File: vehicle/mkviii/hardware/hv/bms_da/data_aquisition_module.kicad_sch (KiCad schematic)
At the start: 70 parts, among them J2 CONN_pcie_x4, U1 LTC1380IGN, U2 LTC1380IGN, U3 LTC1380IGN, U4 LTC1380IGN, U5 MCP6001T-I-LT, U6 MCP6001T-I-LT, U7 MCP6001T-I-LT, U8 MCP6001T-I-LT

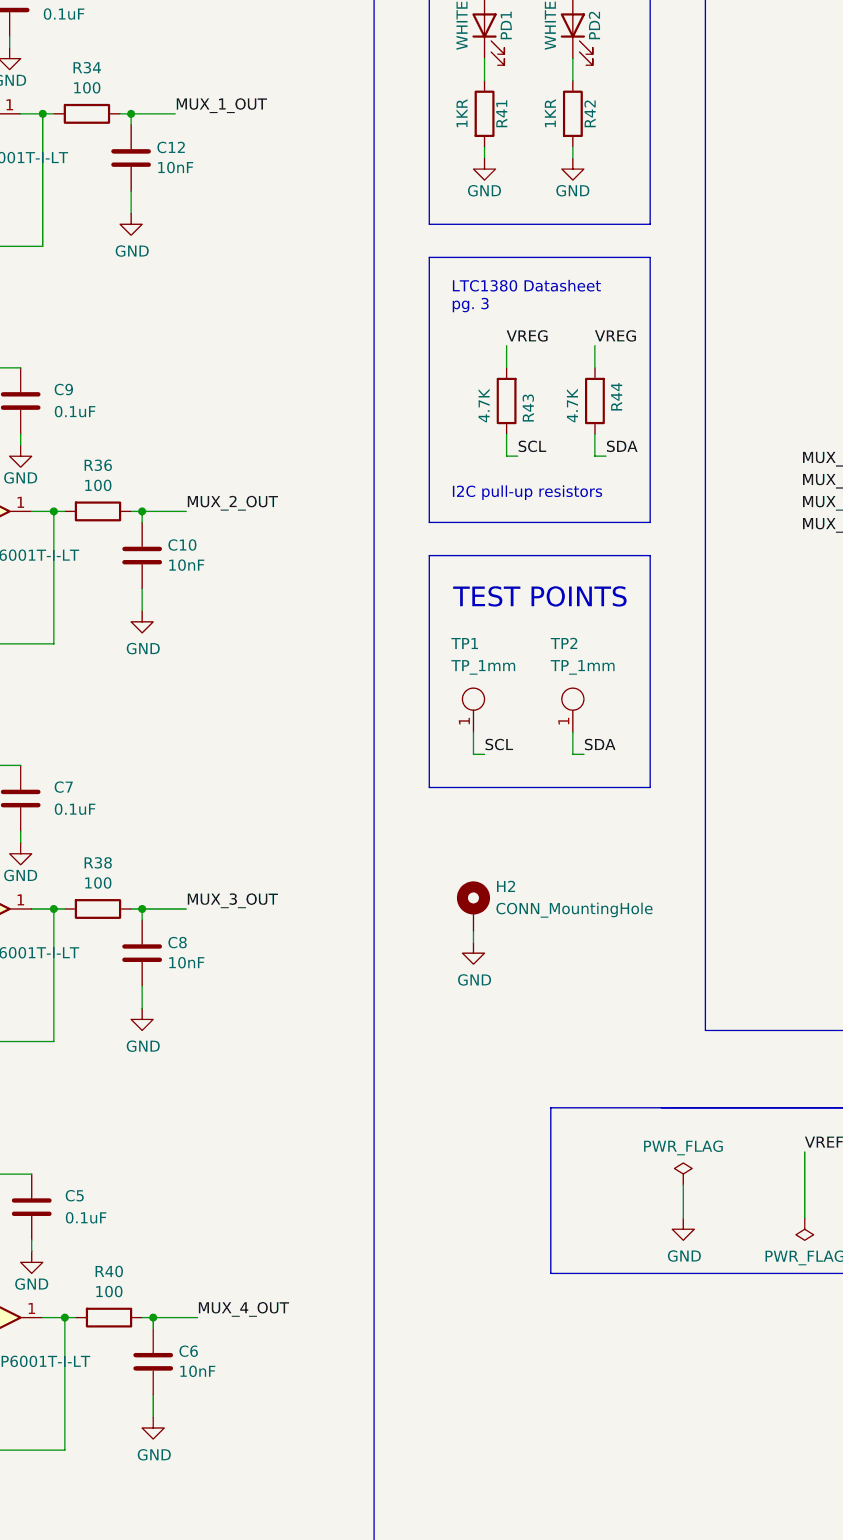
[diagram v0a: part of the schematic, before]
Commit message: Fixed wrong resistor values for BMS DA SMBus; moved all files to the mkviii folder from mkiii
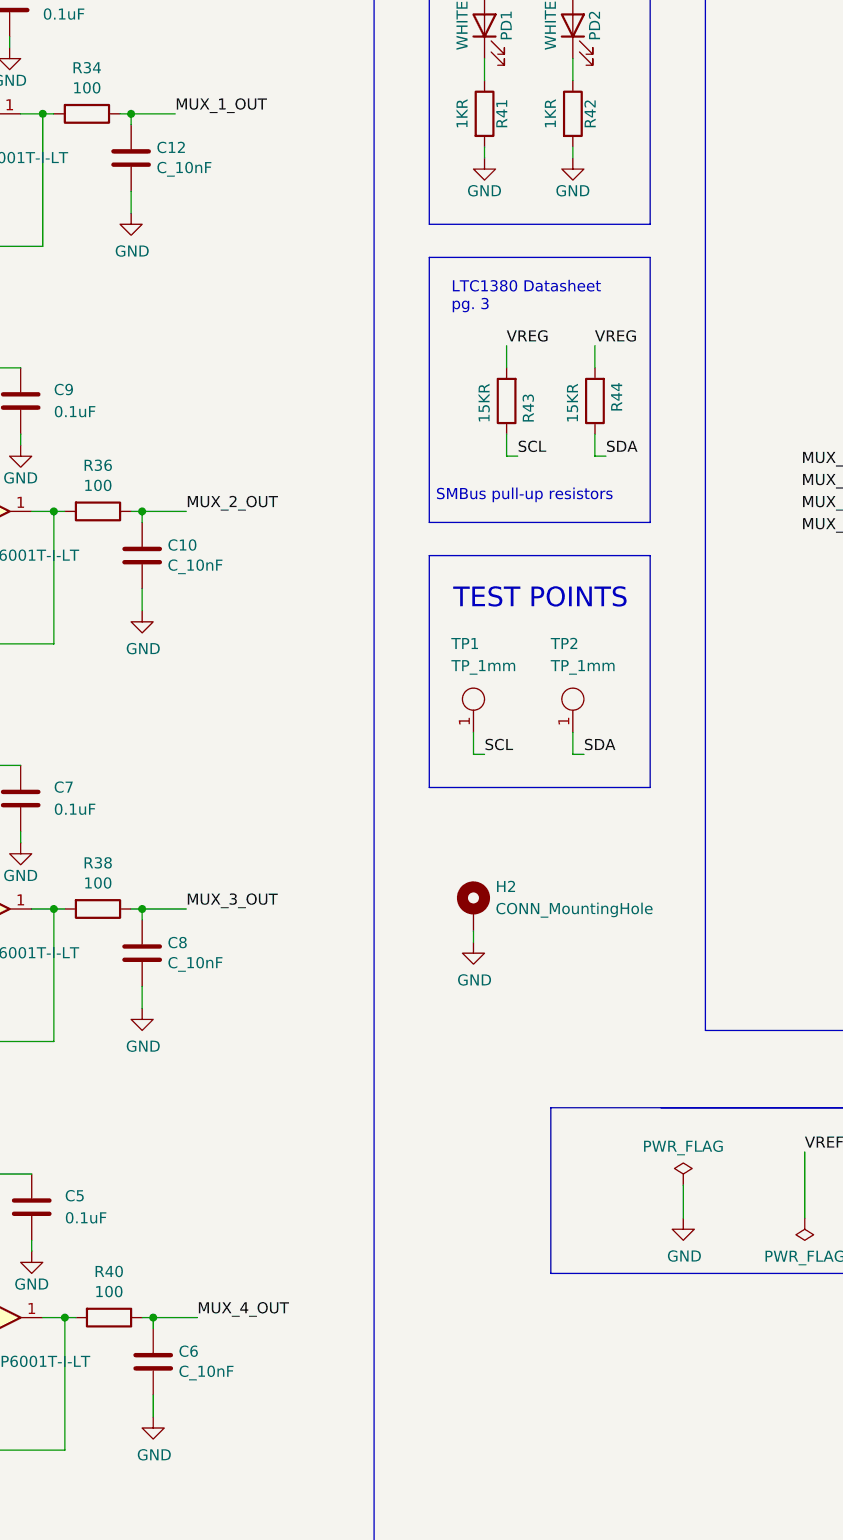
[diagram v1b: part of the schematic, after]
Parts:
- C10, C12, C6, C8: value 10nF -> C_10nF
- R43, R44: value 4.7K -> 15KR
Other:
- note added: "SMBus pull-up resistors"
- note removed: "I2C pull-up resistors"
- title: MKVII Data Aquisition Module -> BMS Data Aquisition Module
